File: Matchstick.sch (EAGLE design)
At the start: 26 parts, among them IC1 74HCT125D, J1 M5STICK_PINOUT, J2 JST-SH 4 Position Connector, J3 USB_A_PTH_MALE, U1 M5STAMP PICO

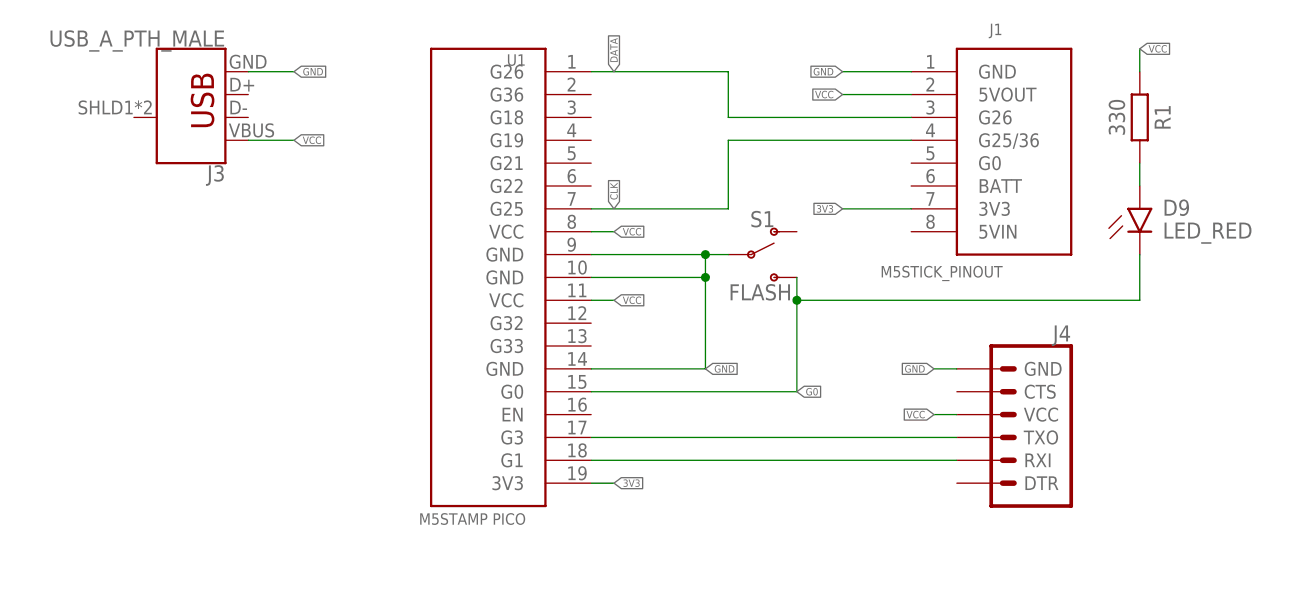
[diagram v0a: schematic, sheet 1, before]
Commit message: Fixing RX/TX cross-wire
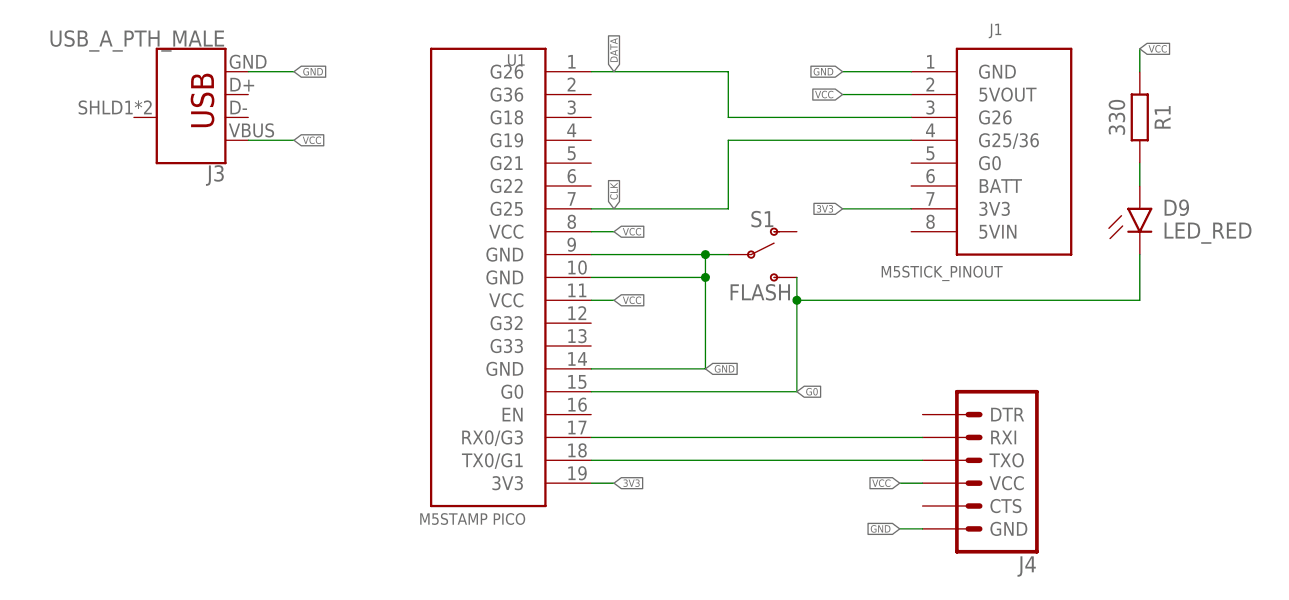
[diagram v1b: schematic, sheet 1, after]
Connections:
- removed net G1: J4.RXI, U1.G1
- removed net G3: J4.TXO, U1.G3
- new net RX: J4.RXI, U1.RX0/G3
- new net TX: J4.TXO, U1.TX0/G1
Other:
- moved on the sheet: J4
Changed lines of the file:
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@@
 <setting verticaltext="up"/>
 </settings>
-<grid distance="0.1" unitdist="inch" unit="inch" style="lines" multiple="1" display="yes" altdistance="0.01" altunitdist="inch" altunit="inch"/>
+<grid distance="0.1" unitdist="inch" unit="inch" style="lines" multiple="1" display="no" altdistance="0.01" altunitdist="inch" altunit="inch"/>
 <layers>
 <layer number="1" name="Top" color="4" fill="1" visible="no" active="no"/>
@@
 <attribute name="SHEET" x="154.305" y="5.08" size="2.54" layer="94"/>
 </instance>
-<instance part="J4" gate="G$1" x="129.54" y="53.34" smashed="yes" rot="MR0">
-<attribute name="VALUE" x="137.16" y="43.434" size="1.778" layer="96" font="vector" rot="MR0"/>
-<attribute name="NAME" x="137.16" y="64.008" size="1.778" layer="95" font="vector" rot="MR0"/>
+<instance part="J4" gate="G$1" x="125.73" y="50.8" smashed="yes" rot="R180">
+<attribute name="VALUE" x="133.35" y="60.706" size="1.778" layer="96" font="vector" rot="R180"/>
+<attribute name="NAME" x="133.35" y="40.132" size="1.778" layer="95" font="vector" rot="R180"/>
 </instance>
 </instances>
@@
 </segment>
 <segment>
-<wire x1="124.46" y1="60.96" x2="121.92" y2="60.96" width="0.1524" layer="91"/>
-<label x="121.92" y="60.96" size="0.8128" layer="95" rot="R180" xref="yes"/>
+<wire x1="120.65" y1="43.18" x2="118.11" y2="43.18" width="0.1524" layer="91"/>
+<label x="118.11" y="43.18" size="0.8128" layer="95" rot="MR0" xref="yes"/>
 <pinref part="J4" gate="G$1" pin="GND"/>
 </segment>
@@
 </segment>
 <segment>
-<wire x1="124.46" y1="55.88" x2="121.92" y2="55.88" width="0.1524" layer="91"/>
-<label x="121.92" y="55.88" size="0.8128" layer="95" rot="R180" xref="yes"/>
+<wire x1="120.65" y1="48.26" x2="118.11" y2="48.26" width="0.1524" layer="91"/>
+<label x="118.11" y="48.26" size="0.8128" layer="95" rot="MR0" xref="yes"/>
 <pinref part="J4" gate="G$1" pin="VCC"/>
 </segment>
@@
 </segment>
 </net>
-<net name="G1" class="0">
-<segment>
-<wire x1="124.46" y1="50.8" x2="83.82" y2="50.8" width="0.1524" layer="91"/>
-<pinref part="U1" gate="G$1" pin="G1"/>
-<pinref part="J4" gate="G$1" pin="RXI"/>
-</segment>
-</net>
-<net name="G3" class="0">
-<segment>
-<wire x1="124.46" y1="53.34" x2="83.82" y2="53.34" width="0.1524" layer="91"/>
-<pinref part="U1" gate="G$1" pin="G3"/>
-<pinref part="J4" gate="G$1" pin="TXO"/>
-</segment>
-</net>
 <net name="LED_PWR" class="0">
 <segment>
@@
 </segment>
 </net>
+<net name="RX" class="0">
+<segment>
+<pinref part="U1" gate="G$1" pin="RX0/G3"/>
+<pinref part="J4" gate="G$1" pin="RXI"/>
+<wire x1="83.82" y1="53.34" x2="120.65" y2="53.34" width="0.1524" layer="91"/>
+</segment>
+</net>
+<net name="TX" class="0">
+<segment>
+<pinref part="J4" gate="G$1" pin="TXO"/>
+<pinref part="U1" gate="G$1" pin="TX0/G1"/>
+<wire x1="120.65" y1="50.8" x2="83.82" y2="50.8" width="0.1524" layer="91"/>
+</segment>
+</net>
